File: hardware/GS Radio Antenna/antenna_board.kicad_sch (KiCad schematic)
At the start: 27 parts, among them J1 Conn_01x02_Socket, U10 IRF4905PBF, U11 IRF4905PBF, U12 IRF4905PBF, U2 ESP32-DEVKITC, U3 LM3940IT-3.3/NOPB, U4 TLC5916IN, U5 TLC5916IN, U6 TLC5916IN, U9 IRF4905PBF

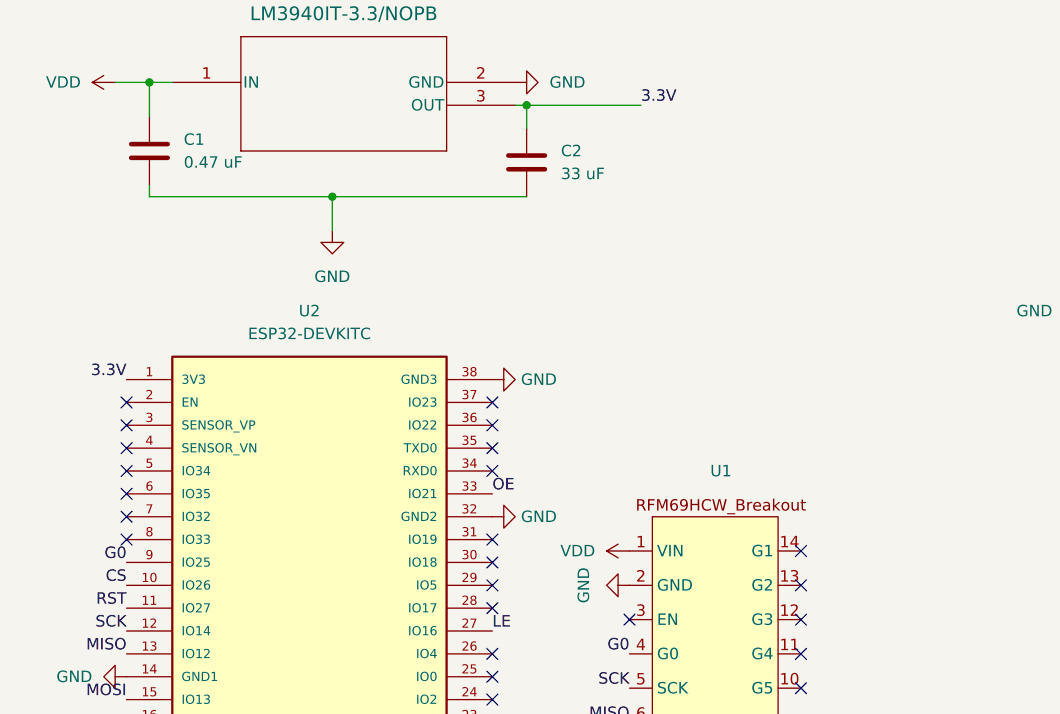
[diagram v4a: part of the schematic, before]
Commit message: Add voltage divider to measure battery voltage
Added a voltage divider and connected it to one of the analog input pins of the ESP32 so we can actually measure the battery voltage
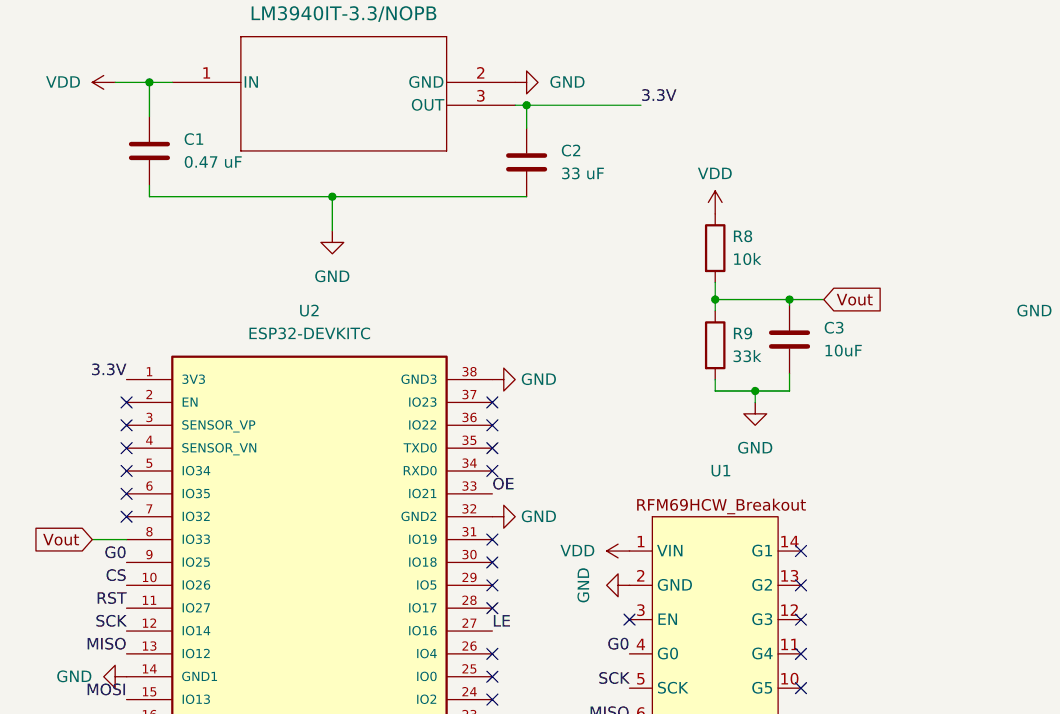
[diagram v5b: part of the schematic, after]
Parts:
- added C3: 10uF, Capacitor_SMD:C_0603_1608Metric_Pad1.08x0.95mm_HandSolder, symbol Device:C
- added R8: 10k, Resistor_SMD:R_0603_1608Metric_Pad0.98x0.95mm_HandSolder, symbol Device:R
- added R9: 33k, Resistor_SMD:R_0603_1608Metric_Pad0.98x0.95mm_HandSolder, symbol Device:R
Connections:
- net GND: now also C3.2, R9.2
- net VDD: now also R8.1
- net Vout: now reaches U2.8 (IO33)
- net Vout: now also C3.1, R8.2, R9.1
- no-connect marks 37 -> 36
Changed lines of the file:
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@@
   (junction (at 31.75 134.62) (diameter 0) (color 0 0 0 0)
   )
+  (junction (at 97.79 62.23) (diameter 0) (color 0 0 0 0)
+  )
   (junction (at 97.79 134.62) (diameter 0) (color 0 0 0 0)
   )
@@
   (junction (at 50.8 40.64) (diameter 0) (color 0 0 0 0)
   )
+  (junction (at 101.6 52.07) (diameter 0) (color 0 0 0 0)
+  )
   (junction (at 97.79 171.45) (diameter 0) (color 0 0 0 0)
   )
   (junction (at 30.48 27.94) (diameter 0) (color 0 0 0 0)
+  )
+  (junction (at 93.345 52.07) (diameter 0) (color 0 0 0 0)
   )
   (no_connect (at 27.94 66.04))
@@
   (no_connect (at 27.94 71.12))
   (no_connect (at 102.87 80.01))
-  (no_connect (at 27.94 78.74))
   (no_connect (at 102.87 91.44))
   (no_connect (at 68.58 63.5))
@@
   (no_connect (at 68.58 86.36))
   (no_connect (at 83.82 87.63))
+  (wire (pts (xy 97.79 62.23) (xy 93.345 62.23))
+    (stroke (width 0) (type default))
+  )
   (wire (pts (xy 93.98 134.62) (xy 97.79 134.62))
     (stroke (width 0) (type default))
@@
     (stroke (width 0) (type default))
   )
+  (wire (pts (xy 93.345 52.07) (xy 101.6 52.07))
+    (stroke (width 0) (type default))
+  )
   (wire (pts (xy 196.85 48.26) (xy 196.85 35.56))
     (stroke (width 0) (type default))
@@
     (stroke (width 0) (type default))
   )
+  (wire (pts (xy 93.345 52.07) (xy 93.345 53.34))
+    (stroke (width 0) (type default))
+  )
+  (wire (pts (xy 24.13 78.74) (xy 27.94 78.74))
+    (stroke (width 0) (type default))
+  )
+  (wire (pts (xy 97.79 63.5) (xy 97.79 62.23))
+    (stroke (width 0) (type default))
+  )
   (wire (pts (xy 31.75 134.62) (xy 35.56 134.62))
     (stroke (width 0) (type default))
@@
     (stroke (width 0) (type default))
   )
+  (wire (pts (xy 101.6 60.325) (xy 101.6 62.23))
+    (stroke (width 0) (type default))
+  )
+  (wire (pts (xy 101.6 62.23) (xy 97.79 62.23))
+    (stroke (width 0) (type default))
+  )
   (wire (pts (xy 93.98 171.45) (xy 97.79 171.45))
     (stroke (width 0) (type default))
@@
     (stroke (width 0) (type default))
   )
+  (wire (pts (xy 101.6 52.07) (xy 105.41 52.07))
+    (stroke (width 0) (type default))
+  )
+  (wire (pts (xy 93.345 62.23) (xy 93.345 60.96))
+    (stroke (width 0) (type default))
+  )
+  (wire (pts (xy 93.345 50.165) (xy 93.345 52.07))
+    (stroke (width 0) (type default))
+  )
   (wire (pts (xy 241.3 48.26) (xy 241.3 35.56))
     (stroke (width 0) (type default))
@@
     (stroke (width 0) (type default))
   )
+  (wire (pts (xy 101.6 52.07) (xy 101.6 52.705))
+    (stroke (width 0) (type default))
+  )
   (wire (pts (xy 232.41 48.26) (xy 241.3 48.26))
     (stroke (width 0) (type default))
@@
   (label "3.3V" (at 34.29 162.56 0) (fields_autoplaced)
     (effects (font (size 1.27 1.27)) (justify left bottom))
+  )
+  (global_label "Vout" (shape input) (at 105.41 52.07 0) (fields_autoplaced)
+    (effects (font (size 1.27 1.27)) (justify left))
+    (property "Intersheetrefs" "${INTERSHEET_REFS}" (at 112.5075 52.07 0)
+      (effects (font (size 1.27 1.27)) (justify left) hide)
+    )
+  )
+  (global_label "Vout" (shape input) (at 24.13 78.74 180) (fields_autoplaced)
+    (effects (font (size 1.27 1.27)) (justify right))
+    (property "Intersheetrefs" "${INTERSHEET_REFS}" (at 17.0325 78.74 0)
+      (effects (font (size 1.27 1.27)) (justify right) hide)
+    )
+  )
+  (symbol (lib_id "power:GND") (at 97.79 63.5 0) (unit 1)
+    (in_bom yes) (on_board yes) (dnp no) (fields_autoplaced)
+    (property "Reference" "#PWR018" (at 97.79 69.85 0)
+      (effects (font (size 1.27 1.27)) hide)
+    )
+    (property "Value" "GND" (at 97.79 68.58 0)
+      (effects (font (size 1.27 1.27)))
+    )
+    (property "Footprint" "" (at 97.79 63.5 0)
+      (effects (font (size 1.27 1.27)) hide)
+    )
+    (property "Datasheet" "" (at 97.79 63.5 0)
+      (effects (font (size 1.27 1.27)) hide)
+    )
+    (pin "1")
+    (instances
+      (project "antenna_board"
+        (path "/61096121-d89e-4ff3-b26c-bc940a13f838"
+          (reference "#PWR018") (unit 1)
+        )
+      )
+    )
   )
   (symbol (lib_id "power:VDD") (at 83.82 80.01 90) (unit 1)
@@
     )
   )
+  (symbol (lib_id "power:VDD") (at 93.345 42.545 0) (unit 1)
+    (in_bom yes) (on_board yes) (dnp no) (fields_autoplaced)
+    (property "Reference" "#PWR017" (at 93.345 46.355 0)
+      (effects (font (size 1.27 1.27)) hide)
+    )
+    (property "Value" "VDD" (at 93.345 38.1 0)
+      (effects (font (size 1.27 1.27)))
+    )
+    (property "Footprint" "" (at 93.345 42.545 0)
+      (effects (font (size 1.27 1.27)) hide)
+    )
+    (property "Datasheet" "" (at 93.345 42.545 0)
+      (effects (font (size 1.27 1.27)) hide)
+    )
+    (pin "1")
+    (instances
+      (project "antenna_board"
+        (path "/61096121-d89e-4ff3-b26c-bc940a13f838"
+          (reference "#PWR017") (unit 1)
+        )
+      )
+    )
+  )
   (symbol (lib_name "CL5641BH_1_1") (lib_id "CL5641BH:CL5641BH_1") (at 205.74 125.73 0) (unit 1)
     (in_bom yes) (on_board yes) (dnp no) (fields_autoplaced)
@@
         (path "/61096121-d89e-4ff3-b26c-bc940a13f838"
           (reference "#PWR06") (unit 1)
+        )
+      )
+    )
+  )
+  (symbol (lib_id "Device:R") (at 93.345 46.355 0) (unit 1)
+    (in_bom yes) (on_board yes) (dnp no) (fields_autoplaced)
+    (property "Reference" "R8" (at 95.25 45.085 0)
+      (effects (font (size 1.27 1.27)) (justify left))
+    )
+    (property "Value" "10k" (at 95.25 47.625 0)
+      (effects (font (size 1.27 1.27)) (justify left))
+    )
+    (property "Footprint" "Resistor_SMD:R_0603_1608Metric_Pad0.98x0.95mm_HandSolder" (at 91.567 46.355 90)
+      (effects (font (size 1.27 1.27)) hide)
+    )
+    (property "Datasheet" "~" (at 93.345 46.355 0)
+      (effects (font (size 1.27 1.27)) hide)
+    )
+    (pin "1")
+    (pin "2")
+    (instances
+      (project "antenna_board"
+        (path "/61096121-d89e-4ff3-b26c-bc940a13f838"
+          (reference "R8") (unit 1)
         )
       )
@@
     )
   )
+  (symbol (lib_id "Device:R") (at 93.345 57.15 0) (unit 1)
+    (in_bom yes) (on_board yes) (dnp no) (fields_autoplaced)
+    (property "Reference" "R9" (at 95.25 55.88 0)
+      (effects (font (size 1.27 1.27)) (justify left))
+    )
+    (property "Value" "33k" (at 95.25 58.42 0)
+      (effects (font (size 1.27 1.27)) (justify left))
+    )
+    (property "Footprint" "Resistor_SMD:R_0603_1608Metric_Pad0.98x0.95mm_HandSolder" (at 91.567 57.15 90)
+      (effects (font (size 1.27 1.27)) hide)
+    )
+    (property "Datasheet" "~" (at 93.345 57.15 0)
+      (effects (font (size 1.27 1.27)) hide)
+    )
+    (pin "1")
+    (pin "2")
+    (instances
+      (project "antenna_board"
+        (path "/61096121-d89e-4ff3-b26c-bc940a13f838"
+          (reference "R9") (unit 1)
+        )
+      )
+    )
+  )
   (symbol (lib_id "TLC5916IN:TLC5916IN") (at 160.02 43.18 0) (unit 1)
     (in_bom yes) (on_board yes) (dnp no) (fields_autoplaced)
@@
         )
       )
+    )
+  )
+  (symbol (lib_id "Device:C") (at 101.6 56.515 0) (unit 1)
+    (in_bom yes) (on_board yes) (dnp no) (fields_autoplaced)
+    (property "Reference" "C3" (at 105.41 55.245 0)
+      (effects (font (size 1.27 1.27)) (justify left))
+    )
+    (property "Value" "10uF" (at 105.41 57.785 0)
+      (effects (font (size 1.27 1.27)) (justify left))
+    )
+    (property "Footprint" "Capacitor_SMD:C_0603_1608Metric_Pad1.08x0.95mm_HandSolder" (at 102.5652 60.325 0)
+      (effects (font (size 1.27 1.27)) hide)
+    )
+    (property "Datasheet" "~" (at 101.6 56.515 0)
+      (effects (font (size 1.27 1.27)) hide)
+    )
+    (pin "1")
+    (pin "2")
+    (instances
+      (project "antenna_board"
+        (path "/61096121-d89e-4ff3-b26c-bc940a13f838"
+          (reference "C3") (unit 1)
+        )
+      )
